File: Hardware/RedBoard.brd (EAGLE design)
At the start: 68.6 x 54.4 mm, 65 parts, among them IC3 LM1117, J1 POWER_JACKOVERPASTE_REDBOARD_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, J2 ICSP, Q1 ZXMP6A13FTA, Q2 2N7002PW, U1 FT231XS, U2 MIC5205, U3 ATMEGA328, Y1 16MHz

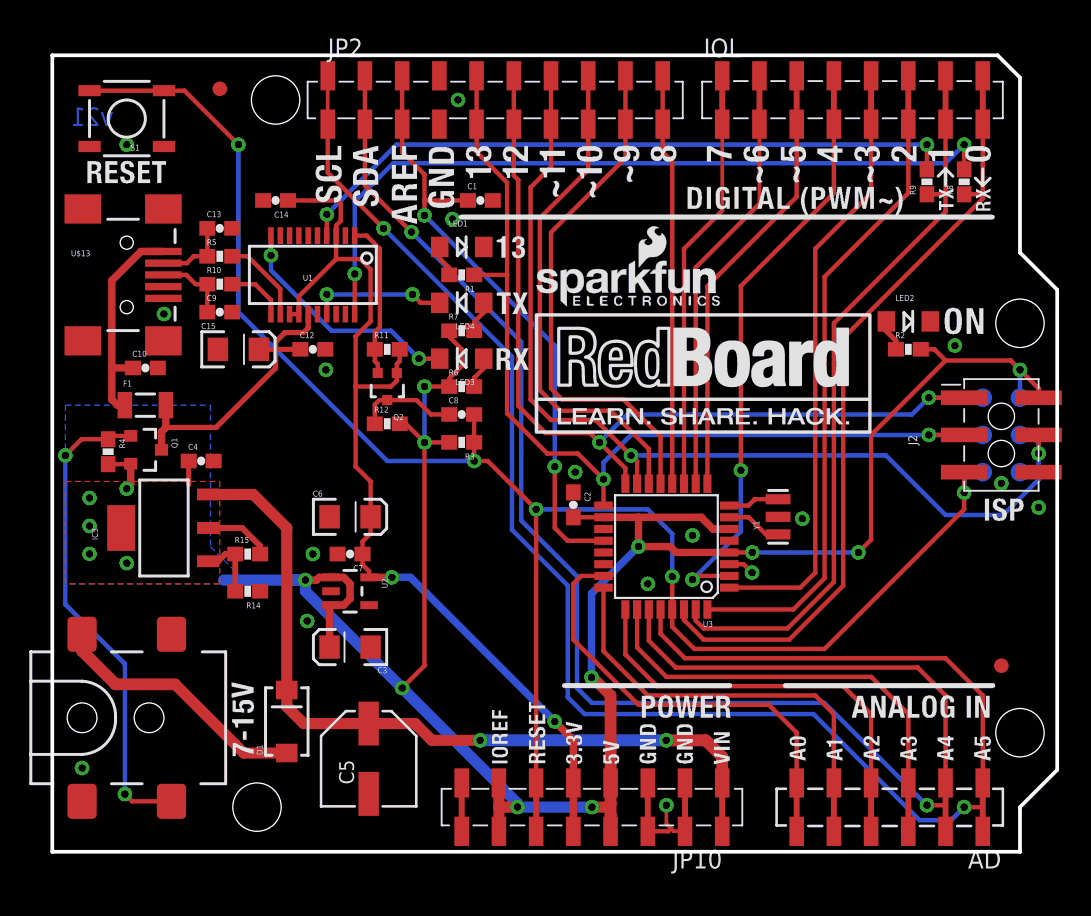
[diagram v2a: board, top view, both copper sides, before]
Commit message: Adjustments to FT231X circuit. Package updates.
- Disconnecting FTDI 3.3V (VCCIO) from ATmega328's 3.3V bus
- Getting rid of MOSFET on DTR line. 5V, 10k pull-up does the job just
fine.
- Adding vias to ISP test points.
- Tailing the dimensions of the board in a bit. Board is now
Arduino-standard 2.1" tall (was 2.14")
- Updating 1x10, 1x08, and 1x06 packages to minimize false DRC errors.
- Updating these packages for QC: resonator, MBRA140 diode, PTC, barrel
jack, reset button.
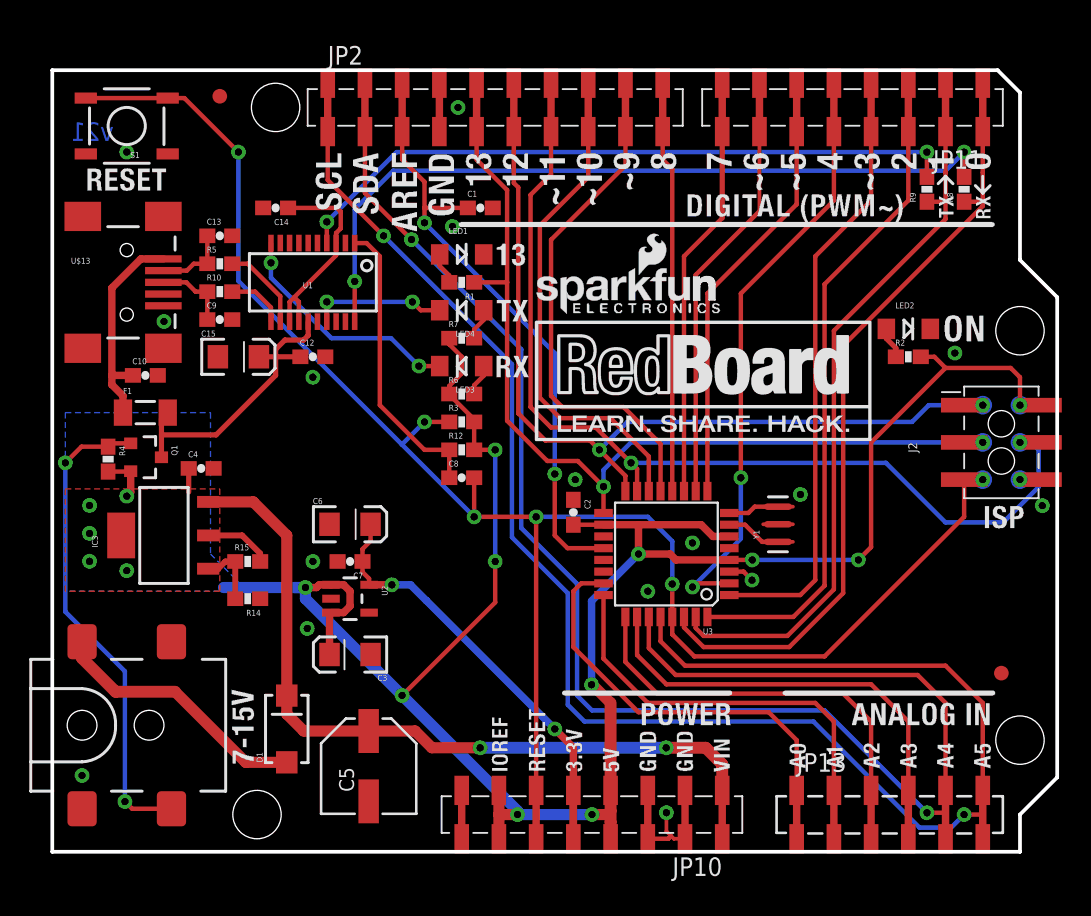
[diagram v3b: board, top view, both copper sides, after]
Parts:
- removed AD: (no value), SparkFun:1X06_SMD_STRAIGHT_COMBO
- removed IOL: (no value), SparkFun:1X08_SMD_COMBINED
- removed J1: POWER_JACKOVERPASTE_REDBOARD_0603, Testing:POWER_JACK_SMD_OVERPASTE_REDBOARD_0603
- removed Q2: 2N7002PW, SparkFun-DiscreteSemi:SOT323
- removed R11: 10k, SparkFun:0603-RES
- added J3: POWER_JACKSUPER_BOMB_DIGITY, Testing:POWER_JACK_SMD_OVERPASTE_SUPER_BOMB_DIGITY
- added JP11: IOL, SparkFun-Connectors:1X08_SMD_COMBINED
- added JP13: AD, SparkFun-Connectors:1X06_SMD_STRAIGHT_COMBO
- D1: device SparkFun:SMA-DIODE -> SparkFun-DiscreteSemi:SMA-DIODE
- F1: device SparkFun:PTC-1206 -> SparkFun-PowerIC:PTC-1206
- S1: device SparkFun:TACTILE_SWITCH_SMD -> SparkFun-Electromechanical:TACTILE-SWITCH-SMD
- moved R12 5.38 mm to (27.9, 27.4)
- moved C8 4.32 mm to (27.9, 25.5)
- moved R3 1.40 mm to (27.9, 29.3), turned to 0 degrees
- moved U$16 1.02 mm to (2.54, 51.3)
- moved C1 0.51 mm to (29.2, 43.9)
- moved C10 0.51 mm to (6.35, 32.5)
- moved C12 0.51 mm to (17.8, 33.8)
- moved C13 0.51 mm to (11.4, 42.0)
- moved C14 0.51 mm to (15.2, 43.9)
- moved C15 0.51 mm to (12.7, 33.8)
- moved C4 0.51 mm to (10.2, 26.2)
- moved JP2 0.51 mm to (18.8, 50.8)
- moved JP6 0.51 mm to (15.2, 50.8)
- moved JP7 0.51 mm to (40.0, 39.4)
- moved JP9 0.51 mm to (11.4, 51.6)
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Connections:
- removed net N$12: Q2.2, R11.1, U1.1
- new net 3V3_FTDI: C14.1, U1.13, U1.14, U1.3
- net 3.3V: now also JP10.5A, JP10.5B; no longer C14.1, JP10.5, Q2.1, R11.2, U1.13, U1.14, U1.3
- net 5V: now also JP10.4A, JP10.4B, JP10.7A, JP10.7B; no longer JP10.4, JP10.7
- net AD0: now also JP13.1A, JP13.1B; no longer AD.1
- net AD1: now also JP13.2A, JP13.2B; no longer AD.2
- net AD2: now also JP13.3A, JP13.3B; no longer AD.3
- net AD3: now also JP13.4A, JP13.4B; no longer AD.4
- net AD4/SDA: now also JP13.5A, JP13.5B; no longer AD.5
- net AD5/SCL: now also JP13.6A, JP13.6B; no longer AD.6
- net DTR: now also U1.1; no longer Q2.3
- net GND: now also J3.GND, JP10.2A, JP10.2B, JP10.3A, JP10.3B; no longer J1.GND, JP10.2, JP10.3
- net INSERT: now also J3.P$4; no longer J1.P$4
- net IO2: now also JP11.3A, JP11.3B; no longer IOL.3
- net IO3: now also JP11.4A, JP11.4B; no longer IOL.4
- net IO4: now also JP11.5A, JP11.5B; no longer IOL.5
- net IO5: now also JP11.6A, JP11.6B; no longer IOL.6
- net IO6: now also JP11.7A, JP11.7B; no longer IOL.7
- net IO7: now also JP11.8A, JP11.8B; no longer IOL.8
- net PWRIN: now also J3.VIN0; no longer J1.VIN0
- net RESET: now also JP10.6A, JP10.6B; no longer JP10.6
- net RX-I: now also JP11.1A, JP11.1B; no longer IOL.1
- net TX-O: now also JP11.2A, JP11.2B; no longer IOL.2
- net VIN: now also JP10.1A, JP10.1B; no longer JP10.1
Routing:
- net 3.3V: track 67.9 -> 29.3 mm
- net 3V3_FTDI: track 0.00 -> 14.4 mm
- net DTR: track 6.92 -> 20.2 mm
- net N$12: track 10.8 -> 0.00 mm
- net MISO: track 62.6 -> 58.2 mm
- net SCK: track 66.6 -> 62.2 mm
- net MOSI: track 69.0 -> 65.7 mm
- net AD5/SCL: track 114.4 -> 111.1 mm
- net SS: track 34.3 -> 31.0 mm
- net IO9: track 35.5 -> 32.2 mm
- net IO8: track 28.1 -> 24.8 mm
- net AREF: track 41.8 -> 38.5 mm
- net AD4/SDA: track 109.4 -> 106.1 mm
- net 5V: track 167.6 -> 165.0 mm
- net RESET: track 120.6 -> 120.9 mm, vias 5 -> 6
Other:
- board size 68.6 x 54.4 mm -> 68.6 x 53.3 mm

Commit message: upping version number to v22`
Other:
- board text added: "v22"
- board text removed: "v21"
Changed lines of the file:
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@@
 <?xml version="1.0" encoding="utf-8"?>
 <!DOCTYPE eagle SYSTEM "eagle.dtd">
-<eagle version="6.5.0">
+<eagle version="6.6.0">
 <drawing>
 <settings>
@@
 <text x="64.77" y="45.593" size="1.4224" layer="26" ratio="12" rot="MR0">MADE IN</text>
 <text x="64.135" y="43.053" size="1.4224" layer="26" ratio="12" rot="MR0">ITALY</text>
-<text x="4.191" y="48.514" size="1.27" layer="16" font="vector" ratio="20" rot="MR0">v21</text>
+<text x="4.191" y="48.514" size="1.27" layer="16" font="vector" ratio="20" rot="MR0">v22</text>
 <text x="32.893" y="-24.13" size="1.778" layer="51" font="vector" ratio="12">J.Lindblom</text>
 <rectangle x1="0.635" y1="22.352" x2="2.032" y2="30.607" layer="43"/>

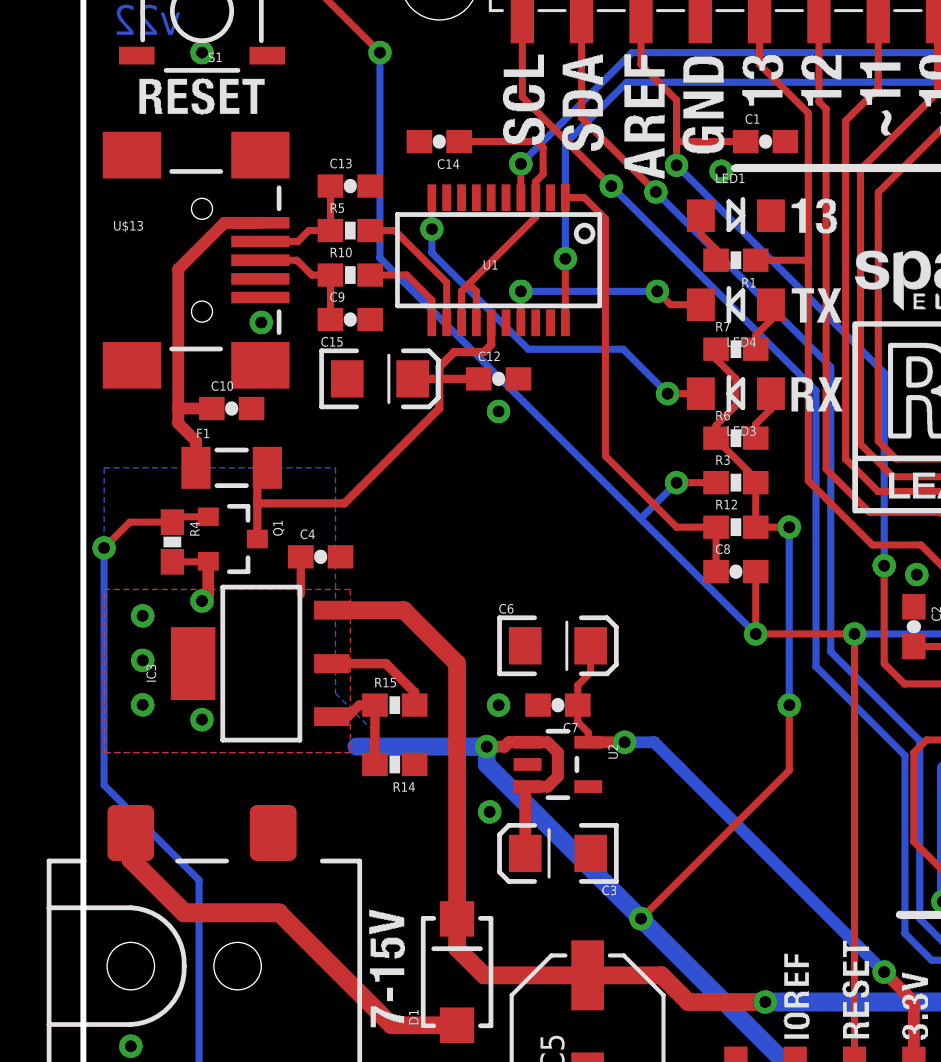
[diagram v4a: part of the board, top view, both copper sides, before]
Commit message: reverting back to old DTR circuit
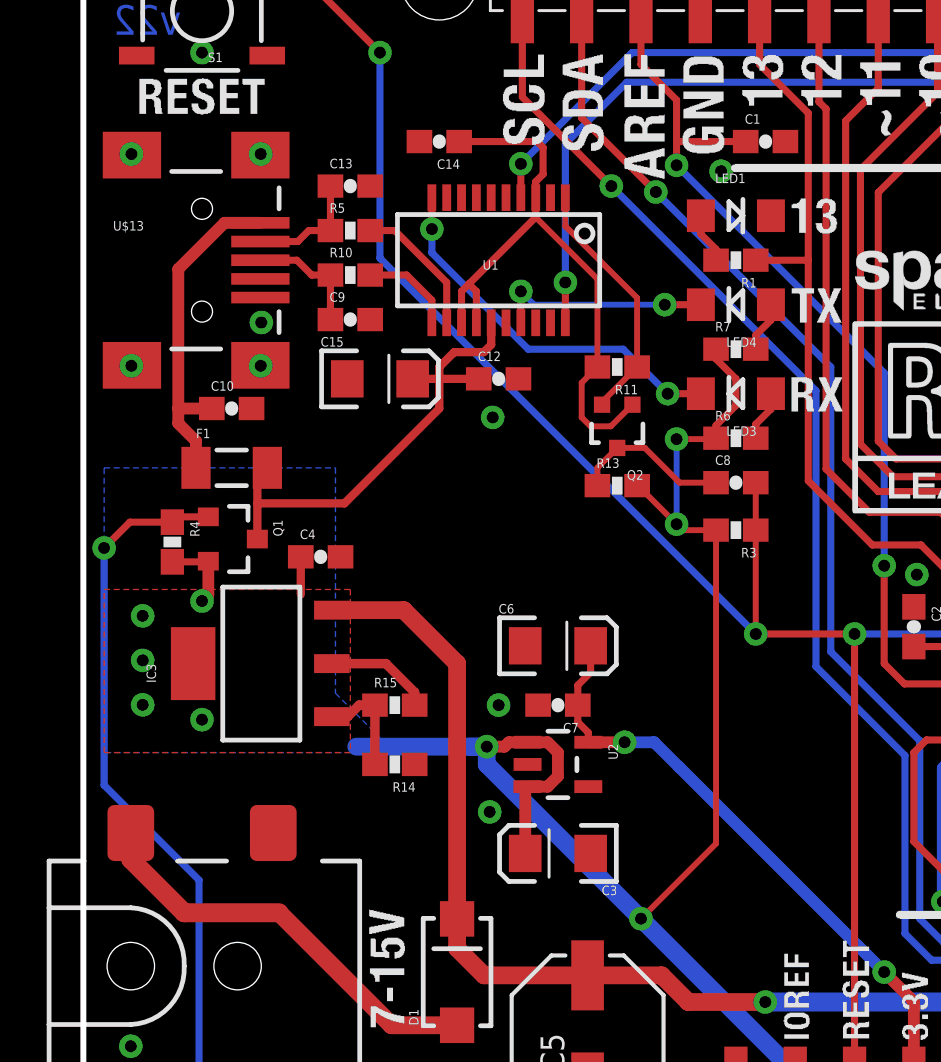
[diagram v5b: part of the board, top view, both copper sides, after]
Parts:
- removed R12: 10k, SparkFun:0603-RES
- added Q2: 2N7002PW, SparkFun-DiscreteSemi:SOT323
- added R11, R13: 10k, SparkFun:0603-RES
- moved FRAME2 15.2 mm to (2.54, -8.89)
- moved C8 3.81 mm to (27.9, 29.3)
- moved R3 2.03 mm to (27.9, 27.3), turned to 180 degrees
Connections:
- removed net 3V3_FTDI: C14.1, U1.13, U1.14, U1.3
- new net 3.3V_F: C14.1, Q2.1, R11.2, U1.13, U1.14, U1.3
- new net FTDI_DTR: Q2.2, R11.1, U1.1
- net 5V: now also R13.2; no longer R12.2
- net DTR: now also Q2.3, R13.1; no longer R12.1, U1.1
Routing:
- net 3.3V_F: track 0.00 -> 27.1 mm
- net 3V3_FTDI: track 14.4 -> 0.00 mm
- net DTR: track 20.2 -> 6.81 mm
- net FTDI_DTR: track 0.00 -> 10.8 mm
- net 5V: track 165.0 -> 167.1 mm
- net RESET: track 120.9 -> 120.8 mm, vias 6 -> 5
- net GND: vias 17 -> 21

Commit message: Schematic cleanup and minor updates post-checklist.
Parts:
- JP1: value LOGO-SFENW2 -> SFE_LOGO_NAME.1_INCH; device SparkFun-Aesthetics:SFE-NEW-WEB -> SparkFun-Aesthetics:SFE_LOGO_NAME_.1
- JP7: value LOGO-SFESK -> SFE_LOGO_FLAME.1_INCH; device SparkFun-Aesthetics:SFE-LOGO-FLAME -> SparkFun-Aesthetics:SFE_LOGO_FLAME_.1
- moved FRAME2 30.5 mm to (1.27, -39.4)
- moved JP7 0.85 mm to (39.3, 39.0)
- moved JP1 0.36 mm to (32.8, 36.4)
- renumbered U$13 to JP12
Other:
- board text added: "Units in inches"
